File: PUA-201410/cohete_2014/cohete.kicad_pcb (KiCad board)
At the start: 2 copper layers, 32.4 x 57.3 mm, 30 parts, among them IC1 ATXMEGA32A4U-A, M1 XBEE-PRO, P1 CONN_2, P2 CONN_4, P3 CONN_6, P4 CONN_4, P5 CONN_8, U1 LM1117, U2 L78S05, X1 CRYSTAL

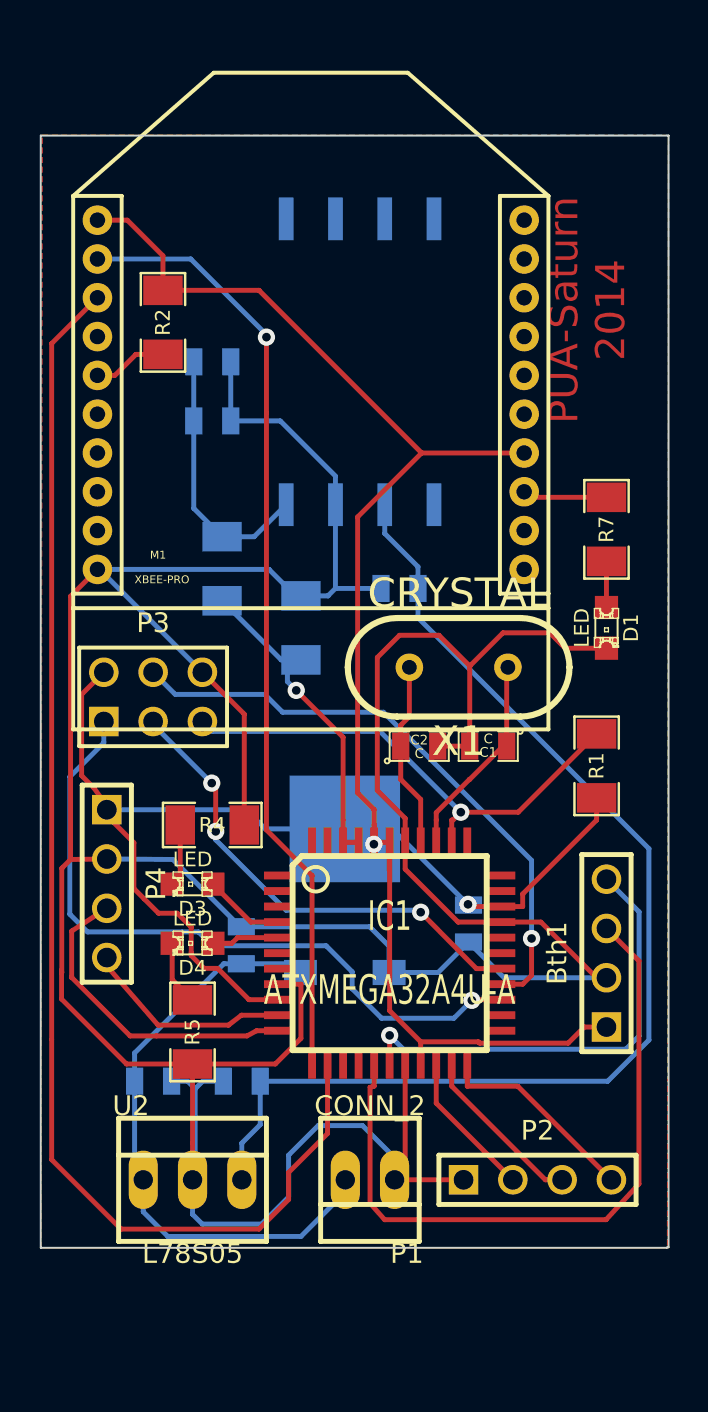
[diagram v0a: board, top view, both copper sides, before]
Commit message: corrección PUA
con resistencias de pulldown y archivos de fabricación
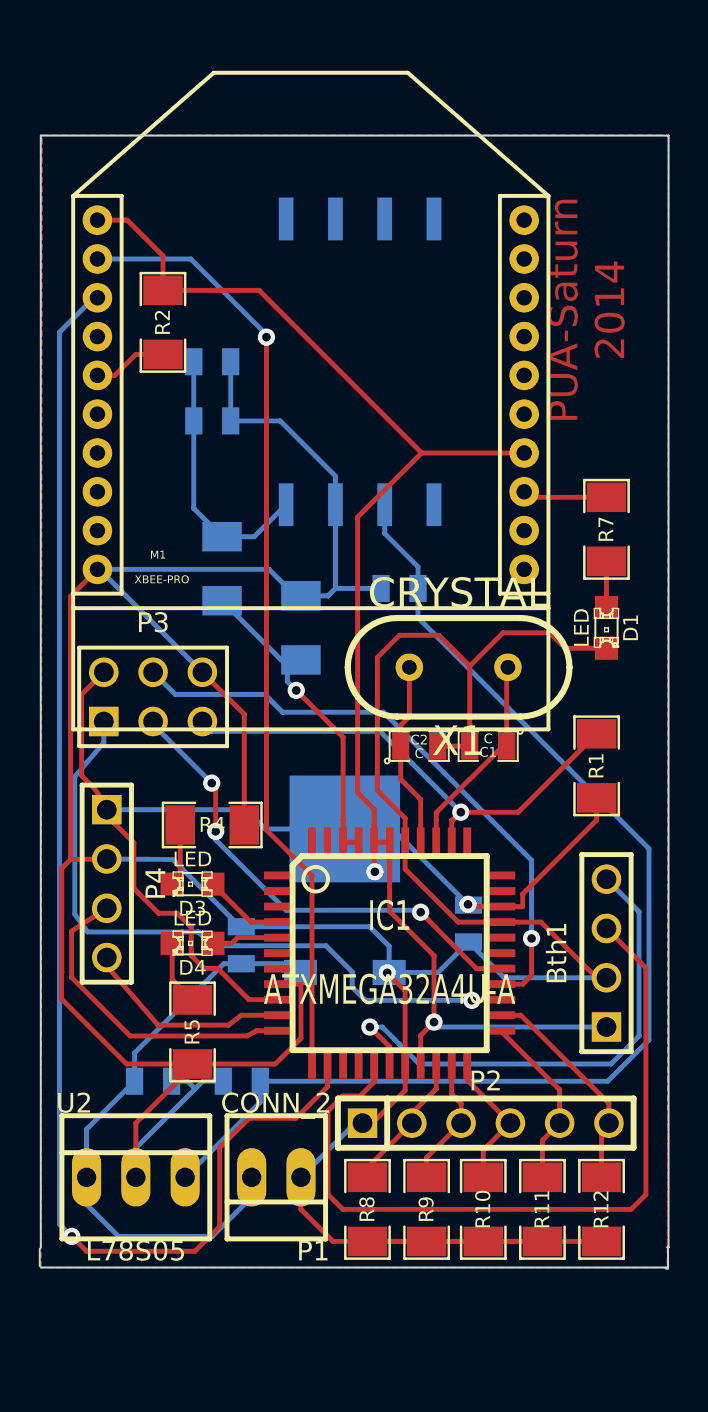
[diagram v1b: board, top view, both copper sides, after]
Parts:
- added R10: 1K, SM1206, F.Cu at (340.1, 237.2)
- added R11: 1K, SM1206, F.Cu at (343.2, 237.2)
- added R12: 1K, SM1206, F.Cu at (346.2, 237.2)
- added R8: 1K, SM1206, F.Cu at (334.1, 237.2)
- added R9: 1K, SM1206, F.Cu at (337.2, 237.2)
- P2: value CONN_4 -> CONN_6; footprint PIN_ARRAY_4x1 -> PIN_ARRAY-6X1
- moved P1 4.83 mm to (329.4, 235.6)
- moved P2 3.96 mm to (340.2, 232.8)
- moved U2 2.92 mm to (322.2, 235.6)
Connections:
- IC1 pad 23: (no net) -> /IGN_3
- IC1 pad 24: (no net) -> /EN_IGN
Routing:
- net GND: track 206.0 -> 221.3 mm, vias 0 -> 1
- net /EN_IGN: track 0.00 -> 11.4 mm
- net /IGN_3: track 0.00 -> 9.19 mm
- net /RX1: track 36.2 -> 39.8 mm
- net /IGN_2: track 10.6 -> 7.34 mm
- net /TX1: track 23.7 -> 26.4 mm
- net /TX0: track 67.5 -> 70.1 mm, vias 0 -> 1
- net /IGN_1: track 8.83 -> 6.78 mm
- net VCC: track 130.4 -> 132.2 mm, vias 2 -> 3
- net /MOSI: track 36.0 -> 34.8 mm
- net +5V: track 59.6 -> 60.7 mm
- net N-0000041: track 31.5 -> 30.5 mm
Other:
- board size 32.4 x 57.3 mm -> 32.4 x 58.4 mm

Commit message: PCB cohete 2014
última versión PCB cohete
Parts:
- added 1PIN: P***, 1pin, F.Cu at (321.0, 242.5)
- added 1PIN: P***, 1pin, F.Cu at (345.0, 242.5)
- added 1PIN: P***, 1pin, F.Cu at (321.0, 181.0)
- added 1PIN: P***, 1pin, F.Cu at (345.0, 181.0)
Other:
- board size 32.4 x 58.4 mm -> 32.3 x 67.4 mm
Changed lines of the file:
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@@
     (area 302.959431 169.362001 352.3654 242.316001)
     (thickness 1.6)
-    (drawings 11)
+    (drawings 10)
     (tracks 342)
     (zones 0)
-    (modules 35)
+    (modules 39)
     (nets 31)
   )
@@
     (22 B.Mask user)
     (23 F.Mask user)
-    (24 Dwgs.User user hide)
+    (24 Dwgs.User user)
     (25 Cmts.User user)
     (26 Eco1.User user)
@@
     (mod_text_size 1 1)
     (mod_text_width 0.15)
-    (pad_size 0.762 2.46126)
-    (pad_drill 0)
+    (pad_size 4.064 4.064)
+    (pad_drill 3.048)
     (pad_to_mask_clearance 0)
     (aux_axis_origin 0 0)
@@
     )
   )
-  (gr_line (start 317.246 239.268) (end 317.246 240.157) (angle 90) (layer Edge.Cuts) (width 0.1))
+  (module 1pin (layer F.Cu)
+    (at 321 242.5)
+    (descr "module 1 pin (ou trou mecanique de percage)")
+    (tags DEV)
+    (path 1pin)
+    (fp_text reference 1PIN (at 0 -3.048) (layer F.SilkS)
+      (effects (font (size 1.016 1.016) (thickness 0.254)))
+    )
+    (fp_text value P*** (at 0 2.794) (layer F.SilkS) hide
+      (effects (font (size 1.016 1.016) (thickness 0.254)))
+    )
+    (fp_circle (center 0 0) (end 0 -2.286) (layer F.SilkS) (width 0.381))
+    (pad 1 thru_hole circle (at 0 0) (size 4.064 4.064) (drill 3.048)
+      (layers *.Cu *.Mask F.SilkS)
+    )
+  )
+  (module 1pin (layer F.Cu)
+    (at 345 242.5)
+    (descr "module 1 pin (ou trou mecanique de percage)")
+    (tags DEV)
+    (path 1pin)
+    (fp_text reference 1PIN (at 0 -3.048) (layer F.SilkS)
+      (effects (font (size 1.016 1.016) (thickness 0.254)))
+    )
+    (fp_text value P*** (at 0 2.794) (layer F.SilkS) hide
+      (effects (font (size 1.016 1.016) (thickness 0.254)))
+    )
+    (fp_circle (center 0 0) (end 0 -2.286) (layer F.SilkS) (width 0.381))
+    (pad 1 thru_hole circle (at 0 0) (size 4.064 4.064) (drill 3.048)
+      (layers *.Cu *.Mask F.SilkS)
+    )
+  )
+  (module 1pin (layer F.Cu)
+    (at 321 181)
+    (descr "module 1 pin (ou trou mecanique de percage)")
+    (tags DEV)
+    (path 1pin)
+    (fp_text reference 1PIN (at 0 -3.048) (layer F.SilkS)
+      (effects (font (size 1.016 1.016) (thickness 0.254)))
+    )
+    (fp_text value P*** (at 0 2.794) (layer F.SilkS) hide
+      (effects (font (size 1.016 1.016) (thickness 0.254)))
+    )
+    (fp_circle (center 0 0) (end 0 -2.286) (layer F.SilkS) (width 0.381))
+    (pad 1 thru_hole circle (at 0 0) (size 4.064 4.064) (drill 3.048)
+      (layers *.Cu *.Mask F.SilkS)
+    )
+  )
+  (module 1pin (layer F.Cu)
+    (at 345 181)
+    (descr "module 1 pin (ou trou mecanique de percage)")
+    (tags DEV)
+    (path 1pin)
+    (fp_text reference 1PIN (at 0 -3.048) (layer F.SilkS)
+      (effects (font (size 1.016 1.016) (thickness 0.254)))
+    )
+    (fp_text value P*** (at 0 2.794) (layer F.SilkS) hide
+      (effects (font (size 1.016 1.016) (thickness 0.254)))
+    )
+    (fp_circle (center 0 0) (end 0 -2.286) (layer F.SilkS) (width 0.381))
+    (pad 1 thru_hole circle (at 0 0) (size 4.064 4.064) (drill 3.048)
+      (layers *.Cu *.Mask F.SilkS)
+    )
+  )
+  (dimension 67.31012 (width 0.3) (layer Dwgs.User)
+    (gr_text 67,310mm (at 313.546272 211.955661 89.89189488) (layer Dwgs.User)
+      (effects (font (size 1.5 1.5) (thickness 0.3)))
+    )
+    (feature1 (pts (xy 317.5 178.308) (xy 312.259775 178.298114)))
+    (feature2 (pts (xy 317.373 245.618) (xy 312.132775 245.608114)))
+    (crossbar (pts (xy 314.83277 245.613208) (xy 314.95977 178.303208)))
+    (arrow1a (pts (xy 314.95977 178.303208) (xy 315.544064 179.430816)))
+    (arrow1b (pts (xy 314.95977 178.303208) (xy 314.371225 179.428603)))
+    (arrow2a (pts (xy 314.83277 245.613208) (xy 315.421315 244.487813)))
+    (arrow2b (pts (xy 314.83277 245.613208) (xy 314.248476 244.4856)))
+  )
+  (dimension 31.62402 (width 0.3) (layer Dwgs.User)
+    (gr_text 31,624mm (at 333.21469 249.12272 0.460197168) (layer Dwgs.User)
+      (effects (font (size 1.5 1.5) (thickness 0.3)))
+    )
+    (feature1 (pts (xy 348.996 245.237) (xy 349.037033 250.345676)))
+    (feature2 (pts (xy 317.373 245.491) (xy 317.414033 250.599676)))
+    (crossbar (pts (xy 317.392347 247.899764) (xy 349.015347 247.645764)))
+    (arrow1a (pts (xy 349.015347 247.645764) (xy 347.89359 248.241213)))
+    (arrow1b (pts (xy 349.015347 247.645764) (xy 347.88417 247.068411)))
+    (arrow2a (pts (xy 317.392347 247.899764) (xy 318.523524 248.477117)))
+    (arrow2b (pts (xy 317.392347 247.899764) (xy 318.514104 247.304315)))
+  )
+  (gr_line (start 317.5 245.618) (end 317.373 245.618) (angle 90) (layer Edge.Cuts) (width 0.1))
+  (gr_line (start 317.5 178.181) (end 317.5 245.618) (angle 90) (layer Edge.Cuts) (width 0.1))
+  (gr_line (start 348.996 178.181) (end 317.5 178.181) (angle 90) (layer Edge.Cuts) (width 0.1))
+  (gr_line (start 348.996 245.618) (end 348.996 178.181) (angle 90) (layer Edge.Cuts) (width 0.1))
+  (gr_line (start 317.373 245.618) (end 348.996 245.618) (angle 90) (layer Edge.Cuts) (width 0.1))
   (gr_line (start 349.631 240.284) (end 349.504 240.284) (angle 90) (layer Edge.Cuts) (width 0.1))
-  (gr_line (start 349.631 239.141) (end 349.631 240.284) (angle 90) (layer Edge.Cuts) (width 0.1))
   (gr_line (start 349.6564 239.1918) (end 349.5802 239.1918) (angle 90) (layer Edge.Cuts) (width 0.1))
-  (gr_line (start 349.6564 181.8894) (end 349.6564 239.1918) (angle 90) (layer Edge.Cuts) (width 0.1))
-  (gr_line (start 317.2968 181.8894) (end 349.6564 181.8894) (angle 90) (layer Edge.Cuts) (width 0.1))
-  (gr_line (start 317.2968 239.2172) (end 317.2968 181.8894) (angle 90) (layer Edge.Cuts) (width 0.1))
-  (gr_line (start 349.5802 240.2332) (end 317.2968 240.2332) (angle 90) (layer Edge.Cuts) (width 0.1))
   (gr_text "PUA-Saturn\n2014" (at 345.4654 190.881 90) (layer F.Cu)
     (effects (font (size 1.5 1.5) (thickness 0.3)))
-  )
-  (dimension 34.544 (width 0.3) (layer Dwgs.User)
-    (gr_text 34,544mm (at 334.264 170.862001) (layer Dwgs.User)
-      (effects (font (size 1.5 1.5) (thickness 0.3)))
-    )
-    (feature1 (pts (xy 351.536 177.292) (xy 351.536 169.512001)))
-    (feature2 (pts (xy 316.992 177.292) (xy 316.992 169.512001)))
-    (crossbar (pts (xy 316.992 172.212001) (xy 351.536 172.212001)))
-    (arrow1a (pts (xy 351.536 172.212001) (xy 350.409497 172.798421)))
-    (arrow1b (pts (xy 351.536 172.212001) (xy 350.409497 171.625581)))
-    (arrow2a (pts (xy 316.992 172.212001) (xy 318.118503 172.798421)))
-    (arrow2b (pts (xy 316.992 172.212001) (xy 318.118503 171.625581)))
-  )
-  (dimension 65.024 (width 0.3) (layer Dwgs.User)
-    (gr_text 65,024mm (at 309.038001 209.804 270) (layer Dwgs.User)
-      (effects (font (size 1.5 1.5) (thickness 0.3)))
-    )
-    (feature1 (pts (xy 316.992 242.316) (xy 307.688001 242.316)))
-    (feature2 (pts (xy 316.992 177.292) (xy 307.688001 177.292)))
-    (crossbar (pts (xy 310.388001 177.292) (xy 310.388001 242.316)))
-    (arrow1a (pts (xy 310.388001 242.316) (xy 309.801581 241.189497)))
-    (arrow1b (pts (xy 310.388001 242.316) (xy 310.974421 241.189497)))
-    (arrow2a (pts (xy 310.388001 177.292) (xy 309.801581 178.418503)))
-    (arrow2b (pts (xy 310.388001 177.292) (xy 310.974421 178.418503)))
   )
   (segment (start 328.6125 230.632) (end 328.6125 231.7115) (width 0.254) (layer B.Cu) (net 1))
@@
     (polygon
       (pts
-        (xy 349.5802 240.2332) (xy 317.2968 240.2332) (xy 317.373 181.864) (xy 349.6564 181.8894) (xy 349.6056 239.2172)
+        (xy 317.5 245.618) (xy 348.996 245.618) (xy 348.869 178.562) (xy 348.869 178.181) (xy 317.5 178.181)
+        (xy 317.373 245.618) (xy 317.5 245.618)
       )
     )
@@
     (polygon
       (pts
-        (xy 349.6056 240.2332) (xy 317.2968 240.2332) (xy 317.3476 181.8894) (xy 349.6564 181.864) (xy 349.6056 239.2172)
+        (xy 317.373 245.618) (xy 348.996 245.618) (xy 348.869 178.181) (xy 317.5 178.181) (xy 317.373 245.618)
       )
     )
